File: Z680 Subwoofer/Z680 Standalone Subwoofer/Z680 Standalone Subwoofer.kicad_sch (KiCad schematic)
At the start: 12 parts, among them J1 Conn_Coaxial, J2 DB15_Female_HighDensity, U1 MC78M05_TO252

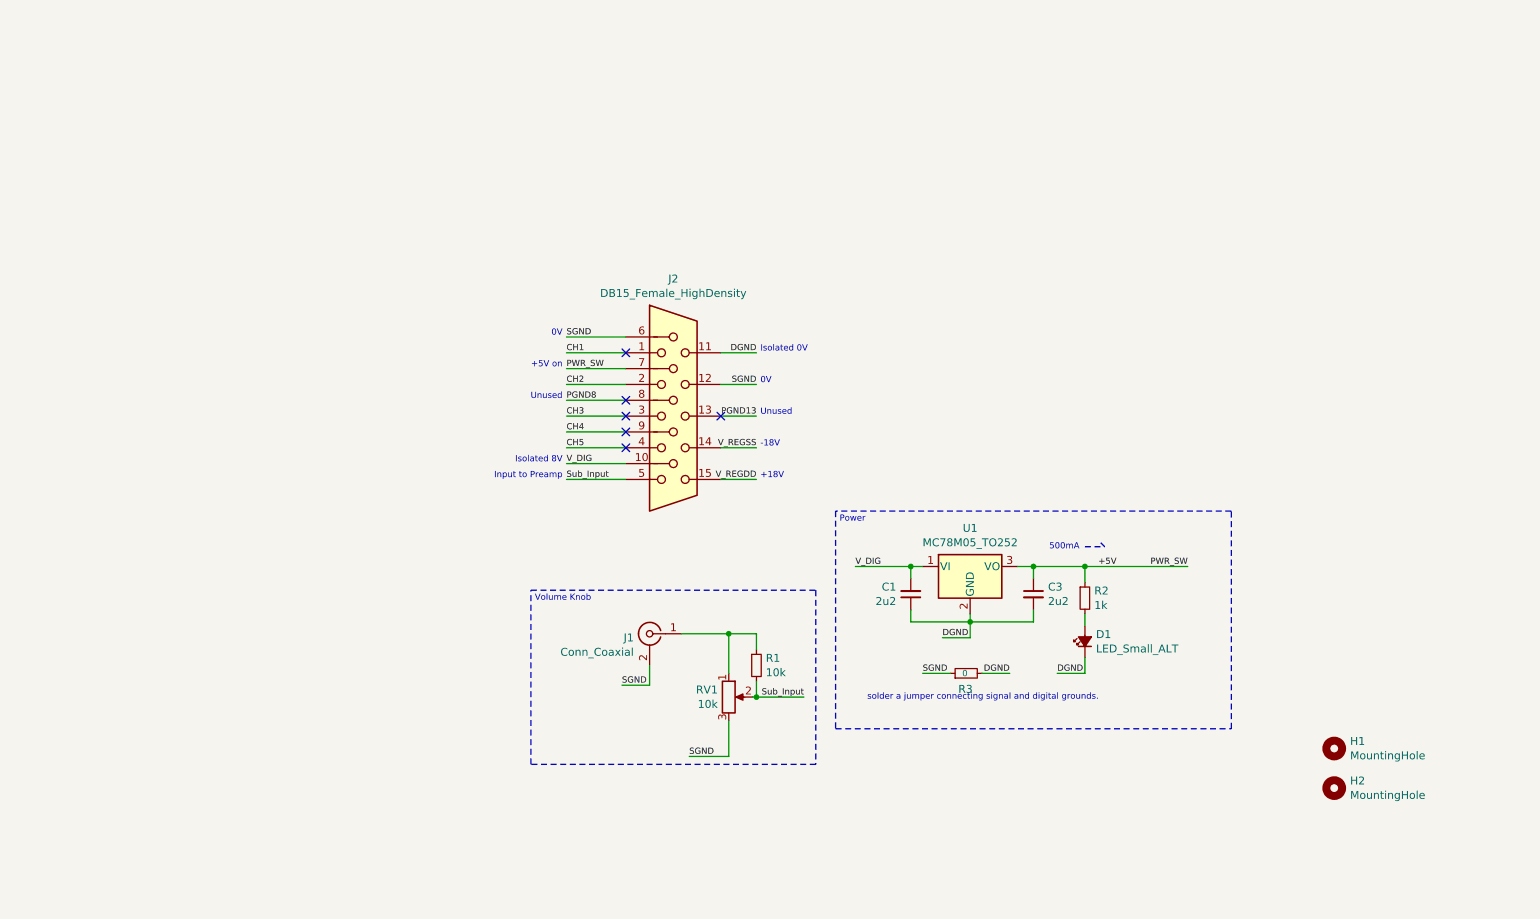
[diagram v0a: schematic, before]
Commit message: Revision 1
Fix low end gain on volume
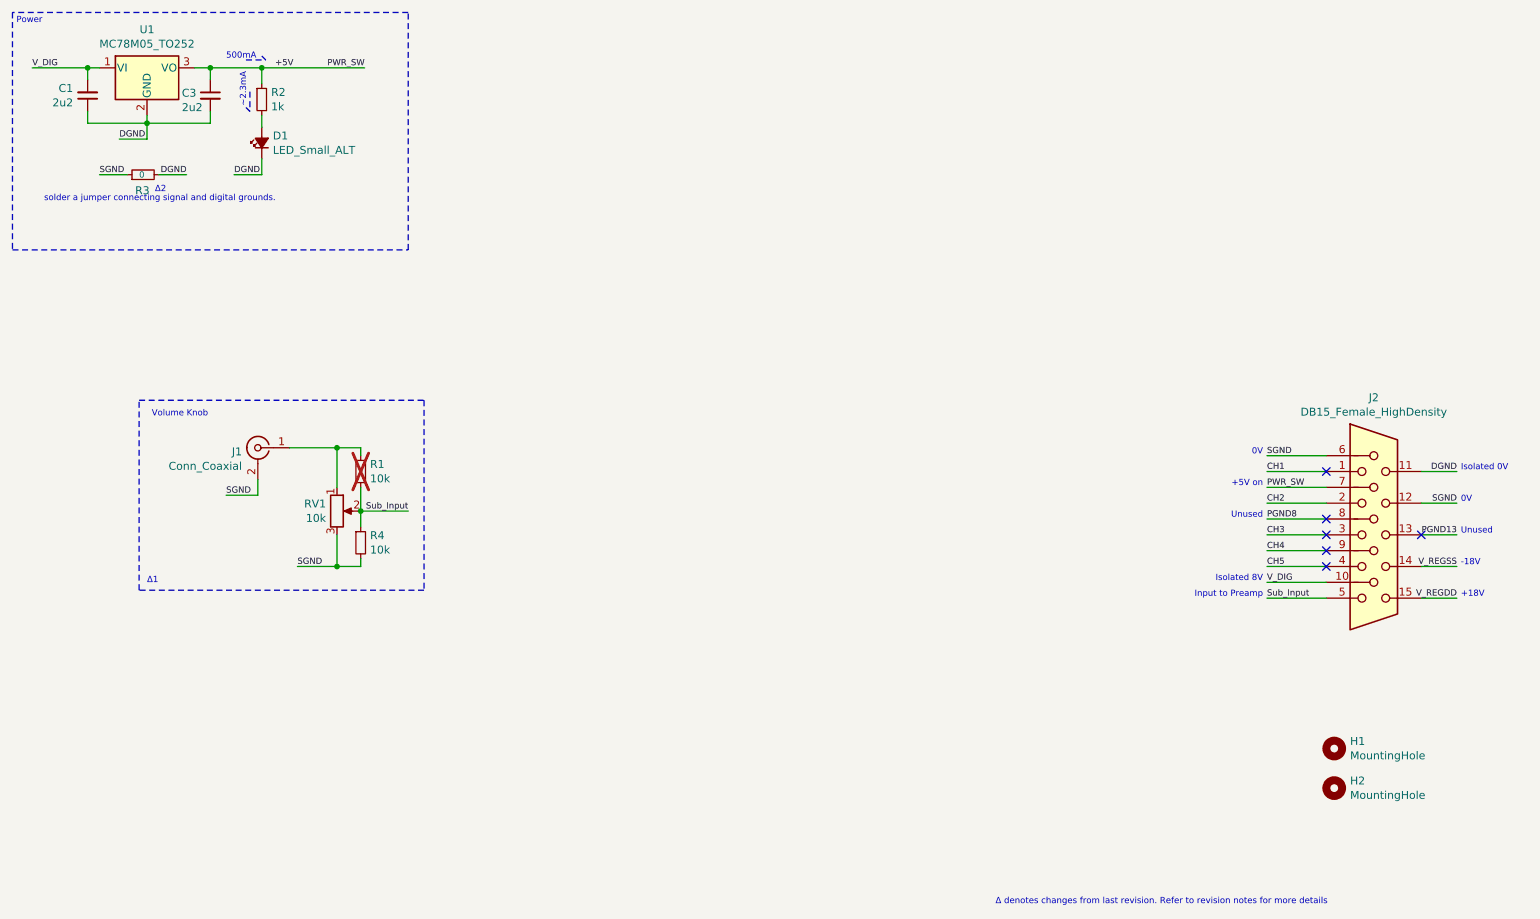
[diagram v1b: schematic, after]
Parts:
- added R4: 10k, Resistor_SMD:R_0603_1608Metric, symbol Device:R_Small
- R1: now not fitted
- R3: footprint Capacitor_SMD:C_0805_2012Metric -> Resistor_SMD:R_0805_2012Metric
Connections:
- net SGND: now also R4.2
- net Sub_Input: now also R4.1
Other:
- note added: "~2.3mA"
- note added: "Δ denotes changes from last revision. Refer to revision notes for more details"
- note added: "Δ1"
- note added: "Δ2"
- moved on the sheet: C1, C3, D1, J1, J2, R2, R3, RV1, U1
